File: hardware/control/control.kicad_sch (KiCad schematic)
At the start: 59 parts, among them J1 Conn_01x05_Male, J2 DCDC-PWM, J3 display, J4 DCDC-MEASURES, J5 CANPWR, J6 CANGND, J7 RJ45, J8 RJ45, J9 Conn_02x03_Odd_Even, Q1 BSS123, SW1 next, SW2 select, U1 2.048V, U2 AP63200WU, U3 PIC18F27Q84, U4 TLE9250VSJXUMA1, Y1 10Mhz

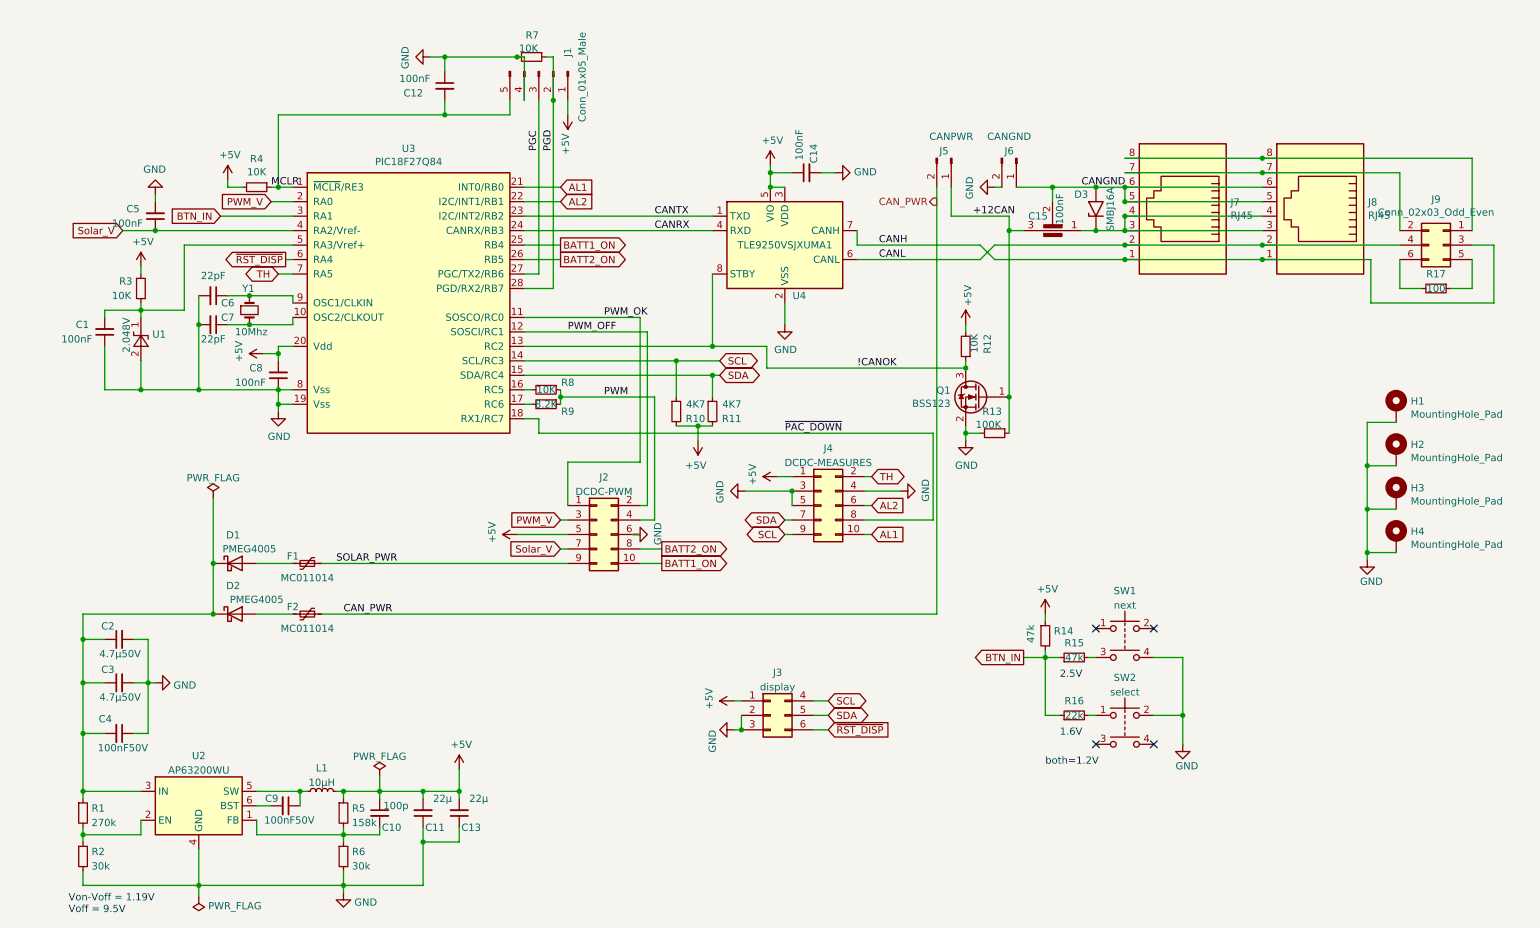
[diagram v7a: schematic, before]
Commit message: Add resistors on pic18 pads connected to DCDC-PWM connector; to protect from spike and accidental short-circuits with solar_power.
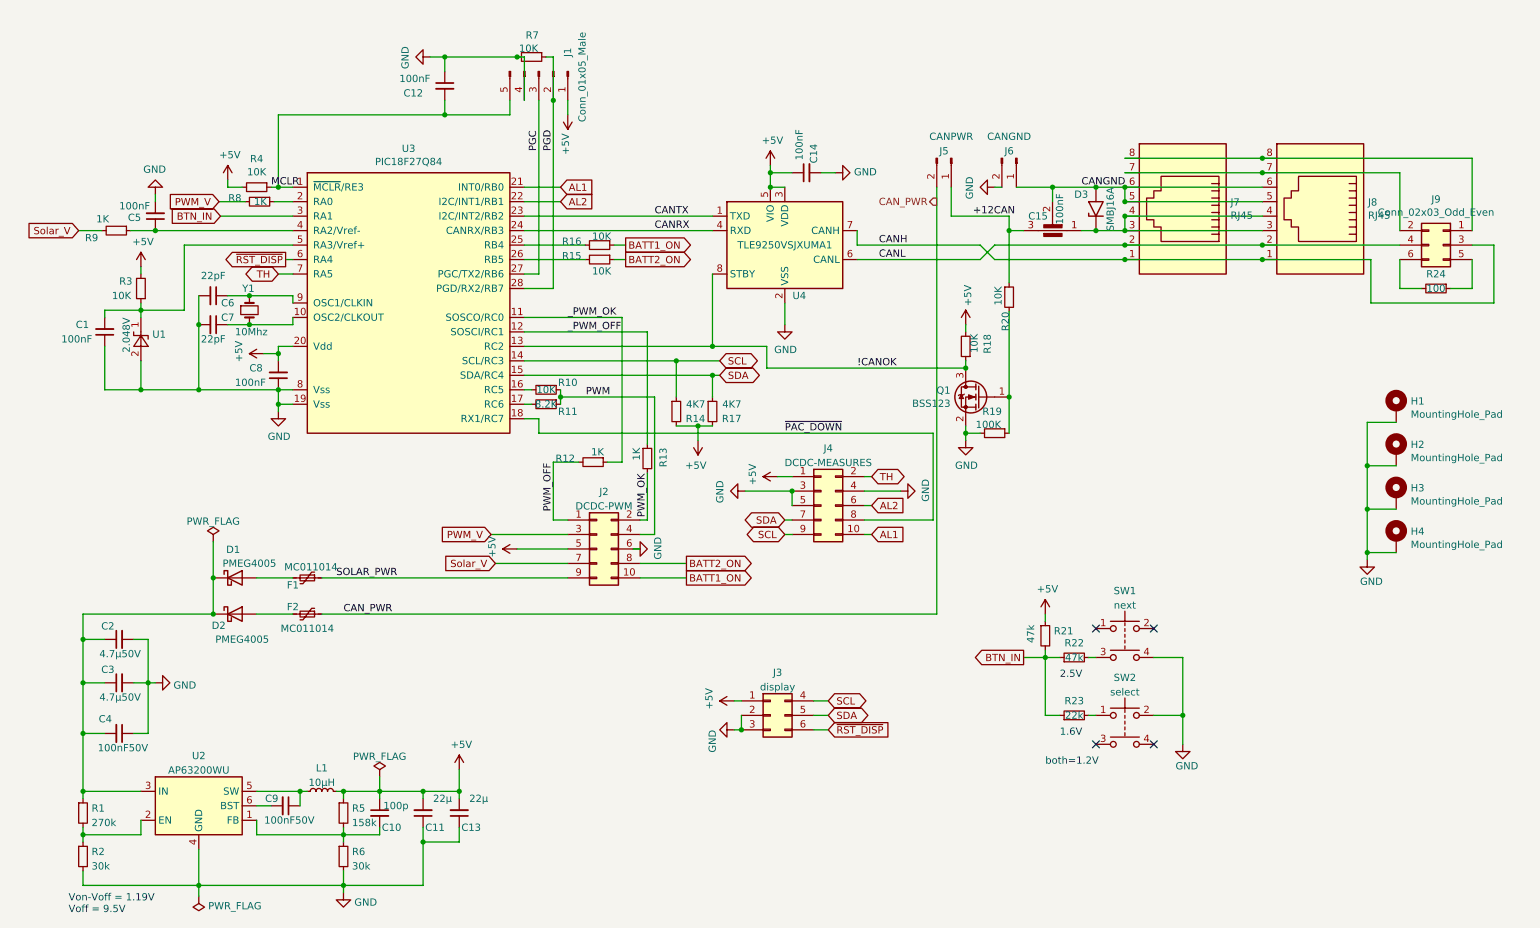
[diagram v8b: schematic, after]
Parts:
- added R12, R13, R8, R9: 1K, Resistor_SMD:R_0805_2012Metric_Pad1.20x1.40mm_HandSolder, symbol Device:R_Small
- added R15, R16, R20: 10K, Resistor_SMD:R_0805_2012Metric_Pad1.20x1.40mm_HandSolder, symbol Device:R_Small
- renumbered R8 to R10, R9 to R11, R10 to R14, R11 to R17, R12 to R18, R13 to R19, R14 to R21, R15 to R22, R16 to R23, R17 to R24
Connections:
- net +12CAN: now also R20.1; no longer Q1.1 (G), R19.1
- net BATT1_ON: now also R16.1; no longer U3.25 (RB4)
- net BATT2_ON: now also R15.1; no longer U3.26 (RB5)
- net PWM_OFF: now also J2.1 (Pin_1), R12.2; no longer J2.2 (Pin_2), U3.12 (SOSCI/RC1)
- net PWM_OK: now also J2.2 (Pin_2), R13.2; no longer J2.1 (Pin_1), U3.11 (SOSCO/RC0)
- net PWM_V: now also R8.2; no longer U3.2 (RA0)
- net Solar_V: now also R9.2; no longer C5.1, U3.4 (RA2/Vref-)
- new net: C5.1, R9.1, U3.4 (RA2/Vref-)
- new net: Q1.1 (G), R19.1, R20.2
- new net: R8.1, U3.2 (RA0)
- new net: R16.2, U3.25 (RB4)
- new net: R15.2, U3.26 (RB5)
- new net _PWM_OFF: R13.1, U3.12 (SOSCI/RC1)
- new net _PWM_OK: R12.1, U3.11 (SOSCO/RC0)
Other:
- moved on the sheet: D1, F1, J2
